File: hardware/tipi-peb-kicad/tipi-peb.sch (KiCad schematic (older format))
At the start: 46 parts, among them Q1 Q_NPN_BCE, U1 74HCT138, U2 27C256, U3 74HCT244, U4 74HCT244, U5 74HCT244, U6 XC95144XL-TQ100, U7 74HCT245, U8 LM1117-3.3, U9 LM7805_TO220

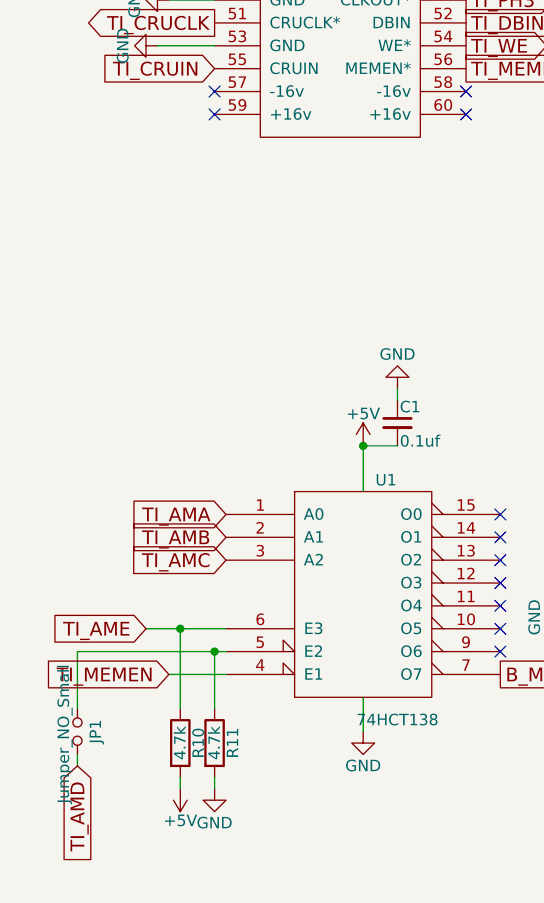
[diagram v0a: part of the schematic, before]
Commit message: Add solder jumpers for genmod vs standard support.
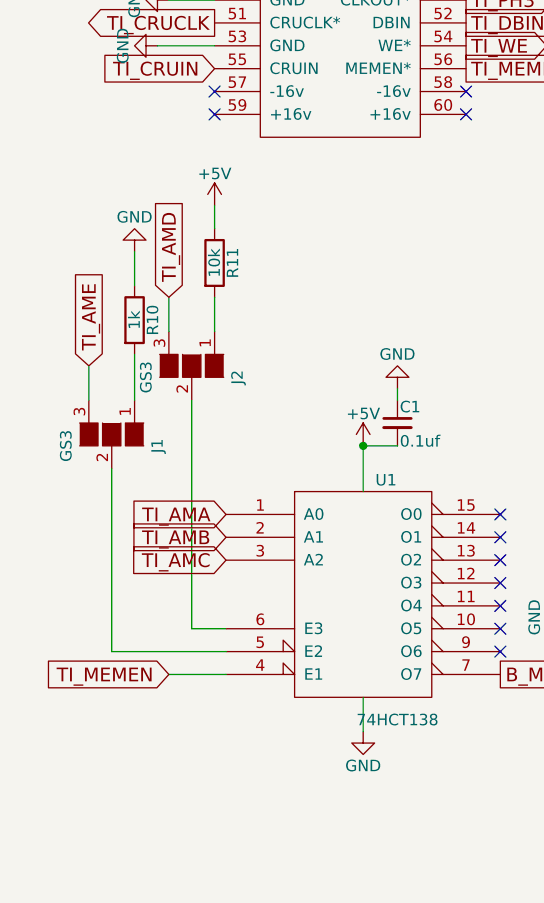
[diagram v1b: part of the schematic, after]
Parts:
- removed JP1: Jumper_NO_Small, Pin_Headers:Pin_Header_Straight_2x01_Pitch2.54mm, symbol Jumper_NO_Small
- added J1, J2: GS3, Connectors:GS3, symbol GS3
- R10: value 4.7k -> 1k
- R11: value 4.7k -> 10k
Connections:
- net +5V: now also R11.1; no longer R10.2
- net GND: now also R10.1; no longer R11.2
- net TI_AMD: now also J2.3 (G3)
- net TI_AME: now also J1.3 (G3); no longer R10.1, U1.6 (E3)
- net at U1.5 (E2): now also J1.2 (G2); no longer R11.1
- new net: J2.2 (G2), U1.6 (E3)
- new net: J1.1 (G1), R10.2
- new net: J2.1 (G1), R11.2
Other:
- moved on the sheet: R10, R11
